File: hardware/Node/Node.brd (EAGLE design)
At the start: 49.5 x 49.5 mm, 71 parts, among them J1 AVR_SPI_PRG_6NS, J2 M04X2, Q1 PMR280UN, Q2 PMR280UN, Q3 PMR280UN, SW1 KSS, SW2 KSS, U1 ATMEGA32U4QFN, U2 BLUETOOTH-RN41", U3 LSM303DLM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

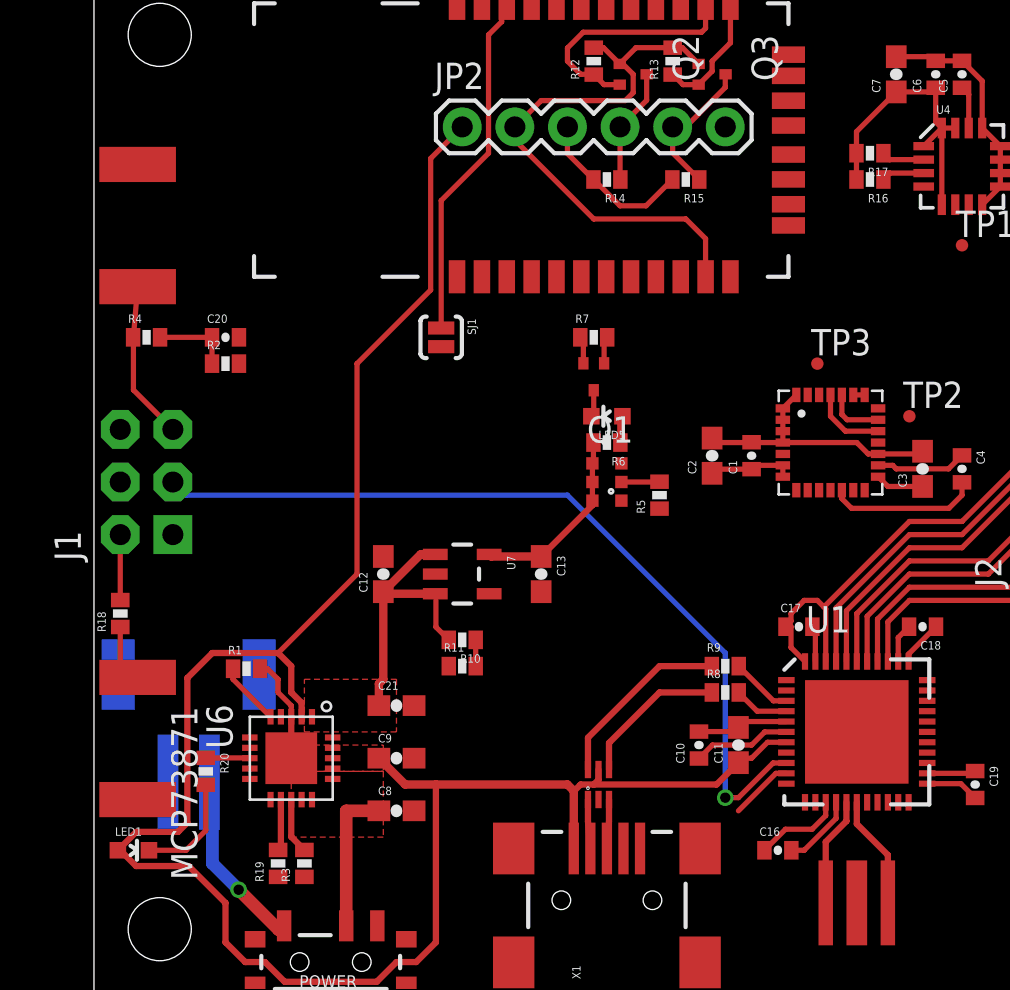
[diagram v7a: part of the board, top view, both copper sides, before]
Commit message: fix packages, route ISP
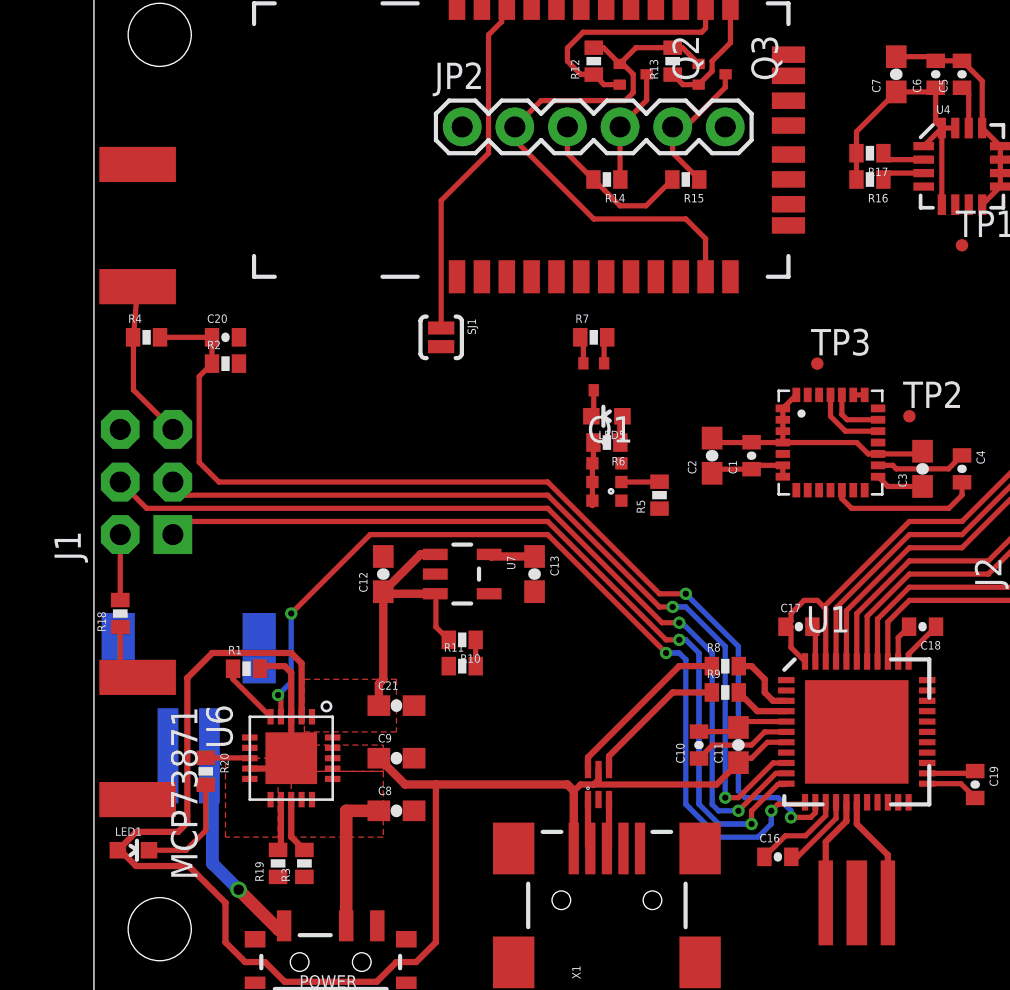
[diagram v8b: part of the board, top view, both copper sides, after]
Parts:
- moved JP1 1.27 mm to (4.57, 15.2)
- moved R8 1.27 mm to (30.5, 15.9)
- moved R9 1.27 mm to (30.5, 14.6)
- moved C16 0.32 mm to (33.0, 6.67)
- moved C13 0.32 mm to (21.3, 20.3)
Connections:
- removed net N$23: R8.2, U1.4
- new net N$15: R8.2, U1.3
- net N$24: now also U1.4; no longer U1.3
- net N$25: now also U9.6; no longer U9.4
- net N$26: now also U9.4; no longer U9.6
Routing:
- net N$27: track 3.79 -> 50.5 mm, vias 0 -> 2
- net PROG2: track 0.00 -> 42.9 mm, vias 0 -> 4
- net MISO: track 0.00 -> 41.4 mm, vias 0 -> 2
- net MOSI: track 3.06 -> 43.8 mm, vias 0 -> 2
- net VBUS: track 100.7 -> 72.0 mm
- net +3V3: track 96.4 -> 92.7 mm
- net N$15: track 0.00 -> 3.38 mm
- net GND: track 45.8 -> 48.7 mm
- net N$23: track 2.69 -> 0.00 mm
- net N$26: track 8.95 -> 6.88 mm
- net N$25: track 7.26 -> 8.39 mm
- net SCK: track 40.7 -> 40.9 mm, vias 1 -> 2
- added copper zone on layer 1, net GND
